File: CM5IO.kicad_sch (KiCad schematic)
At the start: 12 parts, among them J11 USB_C_Receptacle_USB2.0

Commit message: complete first pass at schematic
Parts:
- added D3: D, Diode_SMD:D_0402_1005Metric, symbol Device:D
- added J4: ATX-24, symbol Connector:ATX-24
- added Q1: BS170F, Package_TO_SOT_THT:TO-92L_Wide, symbol Transistor_FET:BS170F
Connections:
- net +3.3v: now also Q1.1 (G)
- net +5v: now also J4.21 (+5V), J4.22 (+5V), J4.23 (+5V), J4.4 (+5V), J4.6 (+5V)
- net GND: now also J4.15 (GND), J4.17 (GND), J4.18 (GND), J4.19 (GND), J4.24 (GND), J4.3 (GND), J4.5 (GND), J4.7 (GND), Q1.2 (S)
- new net: D3.2 (A), J4.16 (PS_ON#), Q1.3 (D)
- new net +12v: J4.10 (+12V), J4.11 (+12V)
- new net +3.3v_pcie: J4.1 (+3.3V), J4.12 (+3.3V), J4.13 (+3.3V), J4.2 (+3.3V)
- new net PWR_BUT: D3.1 (K)
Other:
- sheet CM5_GPIO ( Ethernet, GPIO, SDCARD) ports: added PWR_BUT; removed none
- sheet PCIe-M2 ports: added +12v, +3.3V; removed +5v, PCIE_PWR_EN

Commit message: first pass at layout
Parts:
- D3: footprint Diode_SMD:D_0402_1005Metric -> Diode_SMD:D_SOD-323F
- H1, H6, H7, H8: footprint CM5IO:MountingHole_2.7mm_M2.5_DIN965 -> CM5IO:atx_mountinghole
- J4: footprint (none) -> Connector_Molex:Molex_Mini-Fit_Jr_5566-24A_2x12_P4.20mm_Vertical
- Q1: footprint Package_TO_SOT_THT:TO-92L_Wide -> Package_TO_SOT_SMD:SOT-23
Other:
- sheet CM5_HighSpeed ports: added none; removed PCIE_PWR_EN
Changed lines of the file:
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@@
-	(wire
-		(pts
-			(xy 186.69 72.39) (xy 214.63 72.39)
-		)
-		(stroke
-			(width 0)
-			(type default)
-		)
-	)
 	(wire
 		(pts
@@
 			)
 		)
-		(property "Footprint" "CM5IO:MountingHole_2.7mm_M2.5_DIN965"
+		(property "Footprint" "CM5IO:atx_mountinghole"
 			(at 22.86 165.735 0)
 			(effects
@@
 			)
 		)
-		(property "Footprint" "CM5IO:MountingHole_2.7mm_M2.5_DIN965"
+		(property "Footprint" "CM5IO:atx_mountinghole"
 			(at 43.815 180.975 0)
 			(effects
@@
 			)
 		)
-		(property "Footprint" "CM5IO:MountingHole_2.7mm_M2.5_DIN965"
+		(property "Footprint" "CM5IO:atx_mountinghole"
 			(at 43.815 175.895 0)
 			(effects
@@
 			)
 		)
-		(property "Footprint" "CM5IO:MountingHole_2.7mm_M2.5_DIN965"
+		(property "Footprint" "CM5IO:atx_mountinghole"
 			(at 43.815 170.815 0)
 			(effects
@@
 			)
 		)
-		(property "Footprint" ""
+		(property "Footprint" "Connector_Molex:Molex_Mini-Fit_Jr_5566-24A_2x12_P4.20mm_Vertical"
 			(at 81.28 119.38 0)
 			(effects
@@
 			)
 		)
-		(property "Footprint" "Package_TO_SOT_THT:TO-92L_Wide"
+		(property "Footprint" "Package_TO_SOT_SMD:SOT-23"
 			(at 62.23 121.285 0)
 			(effects
@@
 			)
 		)
-		(property "Footprint" "Diode_SMD:D_0402_1005Metric"
+		(property "Footprint" "Diode_SMD:D_SOD-323F"
 			(at 49.53 106.68 0)
 			(effects
@@
 			)
 		)
-		(property "Datasheet" "~"
+		(property "Datasheet" "https://4donline.ihs.com/images/VipMasterIC/IC/PHGL/PHGL-S-A0001056703/PHGL-S-A0001057188-1.pdf?hkey=6D3A4C79FDBF58556ACFDE234799DDF0"
 			(at 49.53 106.68 0)
 			(effects
@@
 			)
 		)
-		(property "Description" "Diode"
+		(property "Description" "1PS76SB10,115"
 			(at 49.53 106.68 0)
 			(effects
@@
 			)
 		)
-		(pin "PCIE_PWR_EN" output
-			(at 186.69 72.39 0)
-			(effects
-				(font
-					(size 1.27 1.27)
-				)
-				(justify right)
-			)
-		)

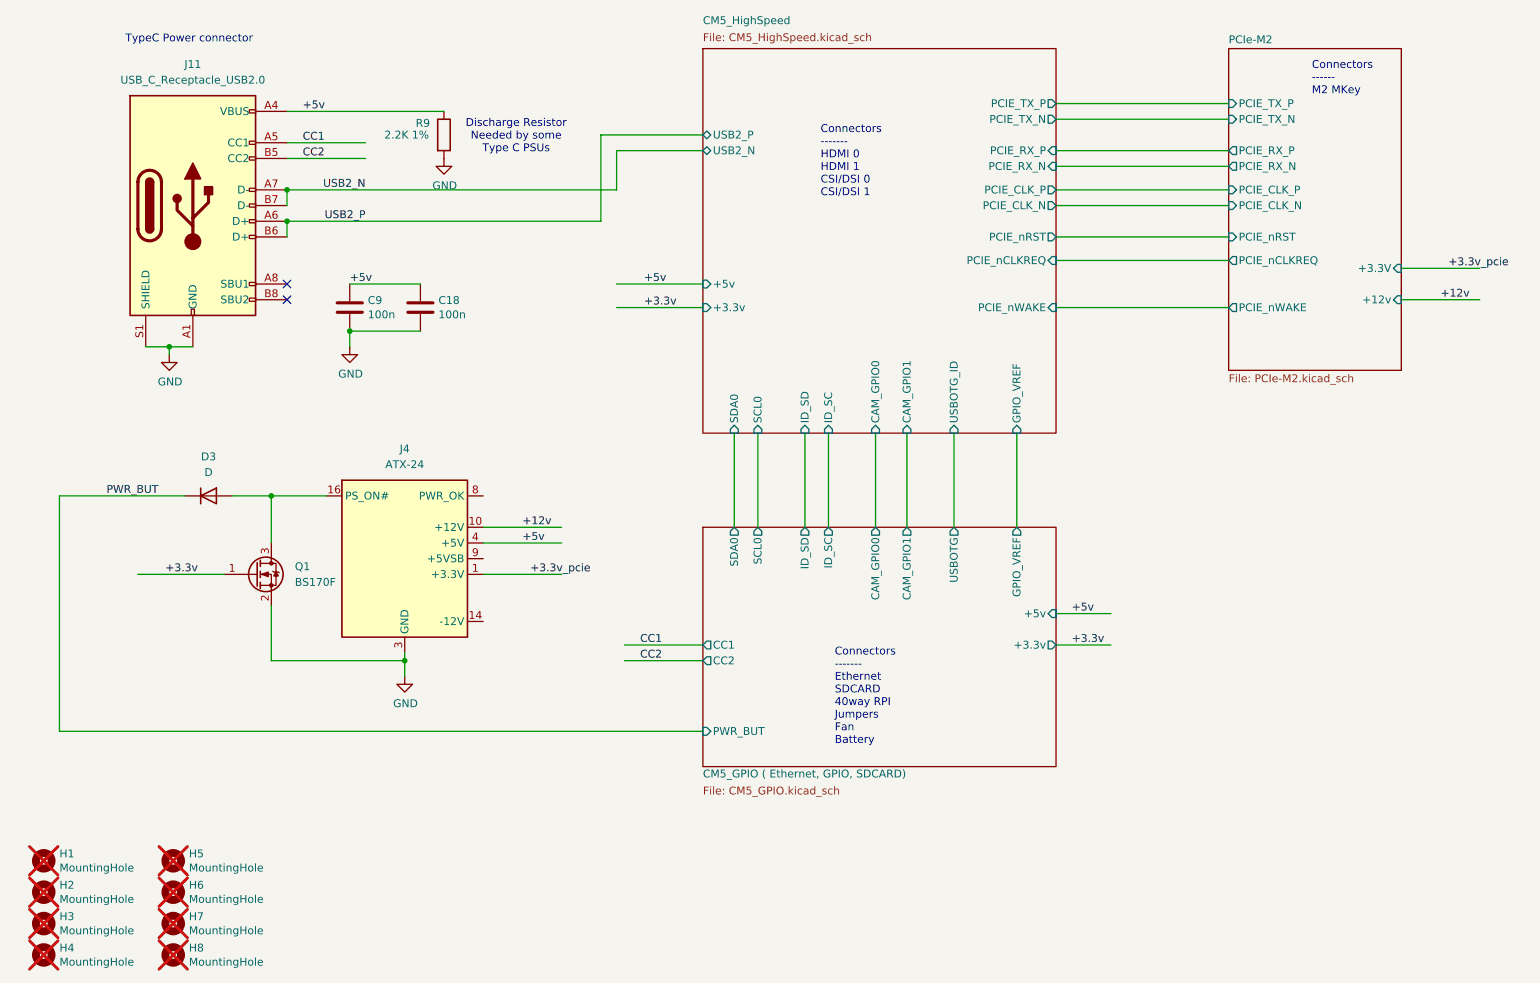
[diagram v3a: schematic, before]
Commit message: fix PCIe position and PS_ON logic
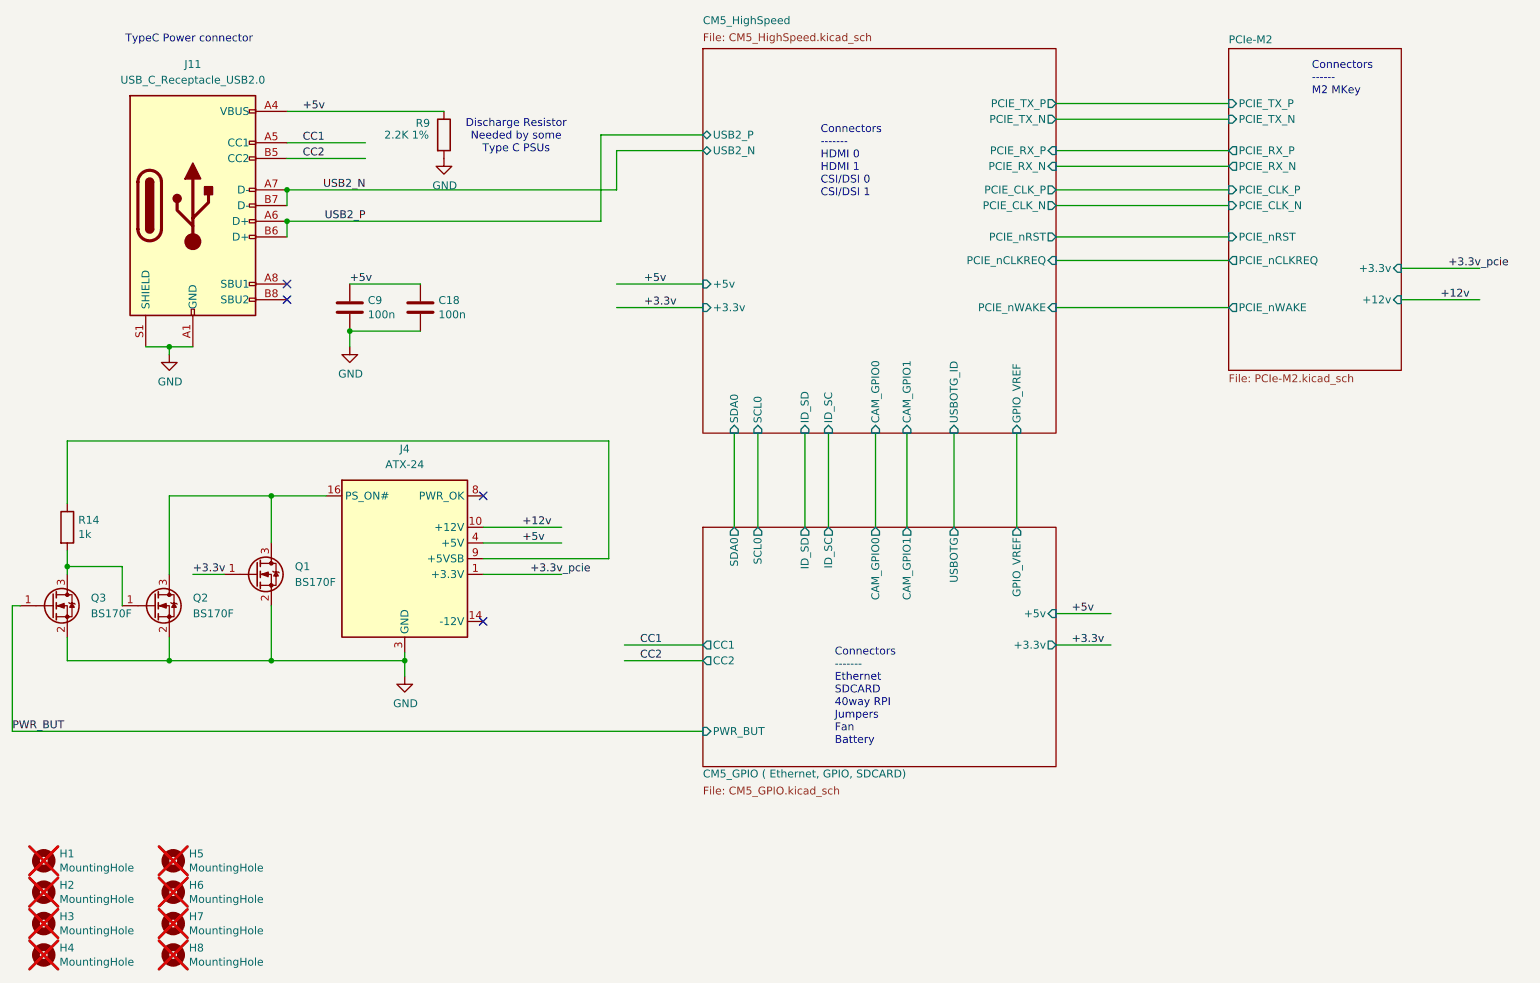
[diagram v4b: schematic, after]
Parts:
- removed D3: D, Diode_SMD:D_SOD-323F, symbol Device:D
- added Q2, Q3: BS170F, Package_TO_SOT_SMD:SOT-23, symbol Transistor_FET:BS170F
- added R14: 1k, Resistor_SMD:R_0402_1005Metric, symbol Device:R
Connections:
- net GND: now also Q2.2 (S), Q3.2 (S)
- net PWR_BUT: now also Q3.1 (G)
- net at J4.16 (PS_ON#), Q1.3 (D): now also Q2.3 (D)
- net at J4.9 (+5VSB): now also R14.1
- new net: Q2.1 (G), Q3.3 (D), R14.2
- no-connect marks 2 -> 4
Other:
- sheet PCIe-M2 ports: added +3.3v; removed +3.3V

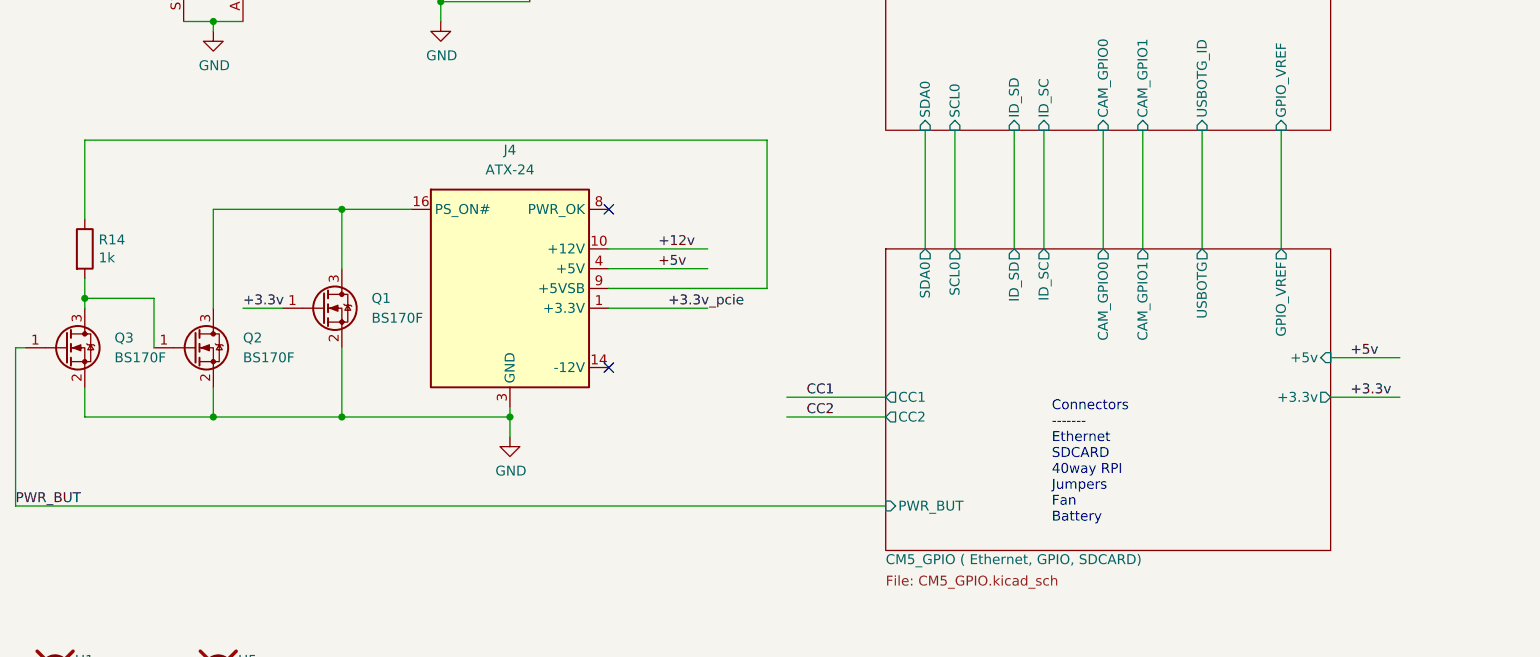
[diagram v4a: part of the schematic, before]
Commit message: add LCSC part numbers, redo fan header and ps_on logic
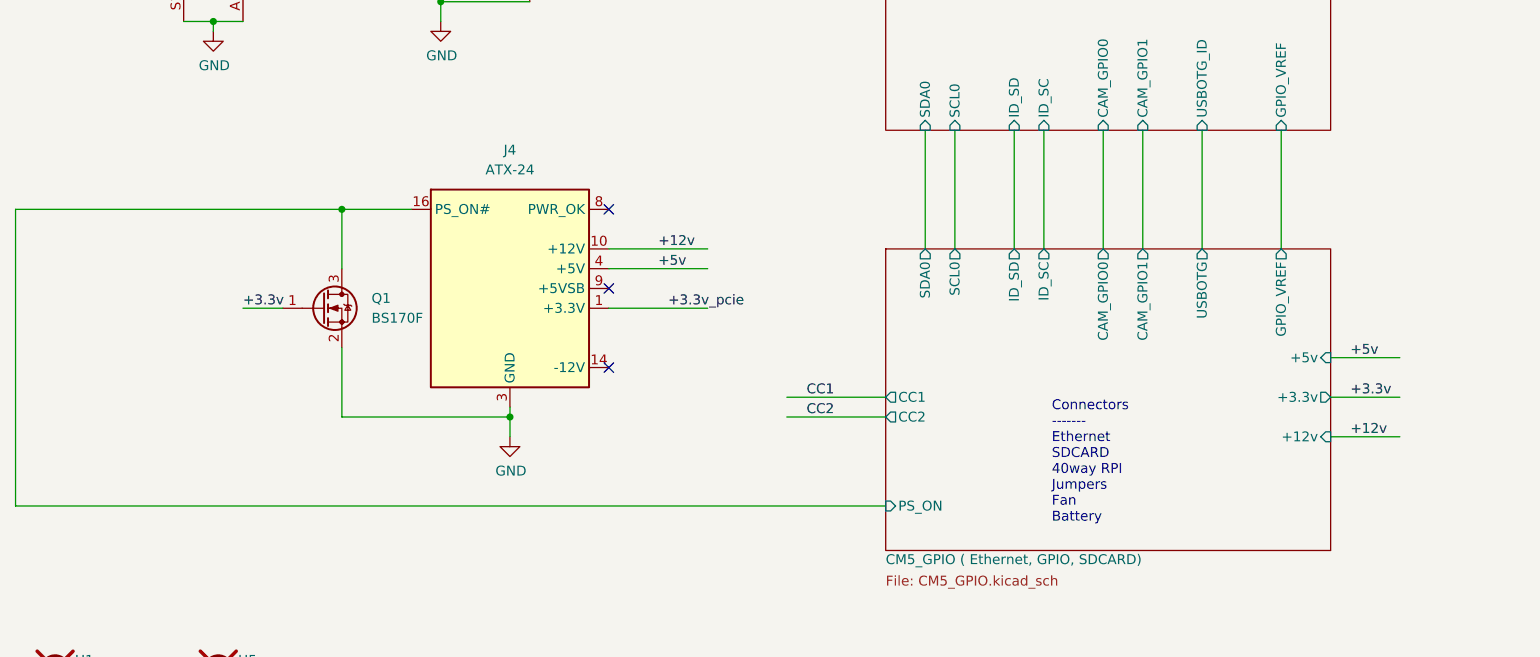
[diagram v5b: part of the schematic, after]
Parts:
- removed Q2, Q3: BS170F, Package_TO_SOT_SMD:SOT-23, symbol Transistor_FET:BS170F
- removed R14: 1k, Resistor_SMD:R_0402_1005Metric, symbol Device:R
- C18, C9: LCSC (none) -> C92753
- J11: LCSC (none) -> C5184243
- J4: LCSC (none) -> C114088
- Q1: LCSC (none) -> C16197299
- R9: LCSC (none) -> C328314
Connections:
- net CM5_GPIO ( Ethernet, GPIO, SDCARD)/PS_ON: now reaches J4.16 (PS_ON#), Q1.3 (D)
- no-connect marks 4 -> 5
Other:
- sheet CM5_GPIO ( Ethernet, GPIO, SDCARD) ports: added +12v, PS_ON; removed PWR_BUT

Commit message: update drop in replacements
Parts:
- J11: mpn (none) -> 629722000214
- J4: footprint Connector_Molex:Molex_Mini-Fit_Jr_5566-24A_2x12_P4.20mm_Vertical -> Connector_Molex:Molex_Mini-Fit_Jr_5566-24A2_2x12_P4.20mm_Vertical; mpn (none) -> 649024221732
- Q1: value BS170F -> MMBT7002K; mpn (none) -> MMBT7002K
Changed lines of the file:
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@@
 (kicad_sch
-	(version 20231120)
+	(version 20250114)
 	(generator "eeschema")
-	(generator_version "8.0")
+	(generator_version "9.0")
 	(paper "A4")
 	(title_block
@@
 		(comment 1 "www.raspberrypi.com")
 	)
+	(text "Connectors\n-------\nEthernet\nSDCARD\n40way RPI\nJumpers\nFan\nBattery"
+		(exclude_from_sim no)
+		(at 150.876 147.066 0)
+		(effects
+			(font
+				(size 1.27 1.27)
+			)
+			(justify left bottom)
+		)
+	)
+	(text "Connectors\n------\nM2 MKey"
+		(exclude_from_sim no)
+		(at 228.092 41.91 0)
+		(effects
+			(font
+				(size 1.27 1.27)
+			)
+			(justify left bottom)
+		)
+	)
+	(text "Discharge Resistor\nNeeded by some\nType C PSUs"
+		(exclude_from_sim no)
+		(at 99.314 48.514 0)
+		(effects
+			(font
+				(size 1.27 1.27)
+			)
+		)
+	)
+	(text "TypeC Power connector"
+		(exclude_from_sim no)
+		(at 36.068 33.528 0)
+		(effects
+			(font
+				(size 1.27 1.27)
+			)
+			(justify left bottom)
+		)
+	)
+	(text "Connectors\n-------\nHDMI 0\nHDMI 1\nCSI/DSI 0\nCSI/DSI 1"
+		(exclude_from_sim no)
+		(at 148.59 58.42 0)
+		(effects
+			(font
+				(size 1.27 1.27)
+			)
+			(justify left bottom)
+		)
+	)
 	(junction
 		(at 43.18 82.55)
@@
 		)
 	)
-	(text "Connectors\n-------\nEthernet\nSDCARD\n40way RPI\nJumpers\nFan\nBattery"
-		(exclude_from_sim no)
-		(at 150.876 147.066 0)
-		(effects
-			(font
-				(size 1.27 1.27)
-			)
-			(justify left bottom)
-		)
-	)
-	(text "Connectors\n------\nM2 MKey"
-		(exclude_from_sim no)
-		(at 228.092 41.91 0)
-		(effects
-			(font
-				(size 1.27 1.27)
-			)
-			(justify left bottom)
-		)
-	)
-	(text "Discharge Resistor\nNeeded by some\nType C PSUs"
-		(exclude_from_sim no)
-		(at 99.314 48.514 0)
-		(effects
-			(font
-				(size 1.27 1.27)
-			)
-		)
-	)
-	(text "TypeC Power connector"
-		(exclude_from_sim no)
-		(at 36.068 33.528 0)
-		(effects
-			(font
-				(size 1.27 1.27)
-			)
-			(justify left bottom)
-		)
-	)
-	(text "Connectors\n-------\nHDMI 0\nHDMI 1\nCSI/DSI 0\nCSI/DSI 1"
-		(exclude_from_sim no)
-		(at 148.59 58.42 0)
-		(effects
-			(font
-				(size 1.27 1.27)
-			)
-			(justify left bottom)
-		)
-	)
 	(label "+5v"
 		(at 72.39 72.39 0)
-		(fields_autoplaced yes)
 		(effects
 			(font
@@
 	(label "CC1"
 		(at 119.38 130.81 0)
-		(fields_autoplaced yes)
 		(effects
 			(font
@@
 	(label "+3.3v"
 		(at 46.99 119.38 0)
-		(fields_autoplaced yes)
 		(effects
 			(font
@@
 	(label "+12v"
 		(at 100.33 111.76 0)
-		(fields_autoplaced yes)
 		(effects
 			(font
@@
 	(label "CC2"
 		(at 119.38 133.35 0)
-		(fields_autoplaced yes)
 		(effects
 			(font
@@
 	(label "+3.3v_pcie"
 		(at 101.6 119.38 0)
-		(fields_autoplaced yes)
 		(effects
 			(font
@@
 	(label "+5v"
 		(at 189.23 125.73 0)
-		(fields_autoplaced yes)
 		(effects
 			(font
@@
 	(label "+5v"
 		(at 120.015 72.39 0)
-		(fields_autoplaced yes)
 		(effects
 			(font
@@
 	(label "USB2_P"
 		(at 74.93 62.23 180)
-		(fields_autoplaced yes)
 		(effects
 			(font
@@
 	(label "CC1"
 		(at 64.77 49.53 0)
-		(fields_autoplaced yes)
 		(effects
 			(font
@@
 	(label "USB2_N"
 		(at 74.93 57.15 180)
-		(fields_autoplaced yes)
 		(effects
 			(font
@@
 	(label "+3.3v"
 		(at 189.23 130.81 0)
-		(fields_autoplaced yes)
 		(effects
 			(font
@@
 	(label "+3.3v"
 		(at 120.015 76.2 0)
-		(fields_autoplaced yes)
 		(effects
 			(font
@@
 	(label "+12v"
 		(at 189.23 135.89 0)
-		(fields_autoplaced yes)
 		(effects
 			(font
@@
 	(label "CC2"
 		(at 64.77 52.07 0)
-		(fields_autoplaced yes)
 		(effects
 			(font
@@
 	(label "+5v"
 		(at 64.77 44.45 0)
-		(fields_autoplaced yes)
 		(effects
 			(font
@@
 	(label "+3.3v_pcie"
 		(at 250.19 69.85 0)
-		(fields_autoplaced yes)
 		(effects
 			(font
@@
 	(label "+5v"
 		(at 100.33 114.3 0)
-		(fields_autoplaced yes)
 		(effects
 			(font
@@
 	(label "+12v"
 		(at 248.92 74.93 0)
-		(fields_autoplaced yes)
 		(effects
 			(font
@@
 			)
 		)
-		(property "Footprint" "Connector_Molex:Molex_Mini-Fit_Jr_5566-24A_2x12_P4.20mm_Vertical"
+		(property "Footprint" "Connector_Molex:Molex_Mini-Fit_Jr_5566-24A2_2x12_P4.20mm_Vertical"
 			(at 81.28 119.38 0)
 			(effects
@@
 			)
 		)
+		(property "mpn" "649024221732"
+			(at 81.28 116.84 0)
+			(effects
+				(font
+					(size 1.27 1.27)
+				)
+				(hide yes)
+			)
+		)
 		(pin "23"
 		)
@@
 			)
 		)
-		(property "Value" "BS170F"
+		(property "Value" "MMBT7002K"
 			(at 63.5 120.6499 0)
 			(effects
@@
 			)
 		)
+		(property "mpn" "MMBT7002K"
+			(at 57.15 119.38 0)
+			(effects
+				(font
+					(size 1.27 1.27)
+				)
+				(hide yes)
+			)
+		)
 		(pin "3"
 		)
@@
 			)
 		)
+		(property "mpn" "629722000214"
+			(at 46.99 59.69 0)
+			(effects
+				(font
+					(size 1.27 1.27)
+				)
+				(hide yes)
+			)
+		)
 		(pin "A1"
 		)
@@
 		(at 129.54 111.76)
 		(size 57.15 38.735)
+		(exclude_from_sim no)
+		(in_bom yes)
+		(on_board yes)
+		(dnp no)
 		(stroke
 			(width 0.1524)
@@
 		(at 129.54 34.29)
 		(size 57.15 62.23)
+		(exclude_from_sim no)
+		(in_bom yes)
+		(on_board yes)
+		(dnp no)
 		(stroke
 			(width 0.1524)
@@
 		(at 214.63 34.29)
 		(size 27.94 52.07)
+		(exclude_from_sim no)
+		(in_bom yes)
+		(on_board yes)
+		(dnp no)
 		(fields_autoplaced yes)
 		(stroke
@@
 		)
 	)
+	(embedded_fonts no)
 )
